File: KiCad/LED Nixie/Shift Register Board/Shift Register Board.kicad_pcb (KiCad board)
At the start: 2 copper layers, 25 x 25 mm, 10 parts, among them J1 Conn_01x04, J2 Conn_01x03, J3 Conn_01x03, J4 Conn_01x01, J5 Conn_01x01, J6 Shift, J7 +5V, J8 GND, U1 74HC595, U2 74HC595

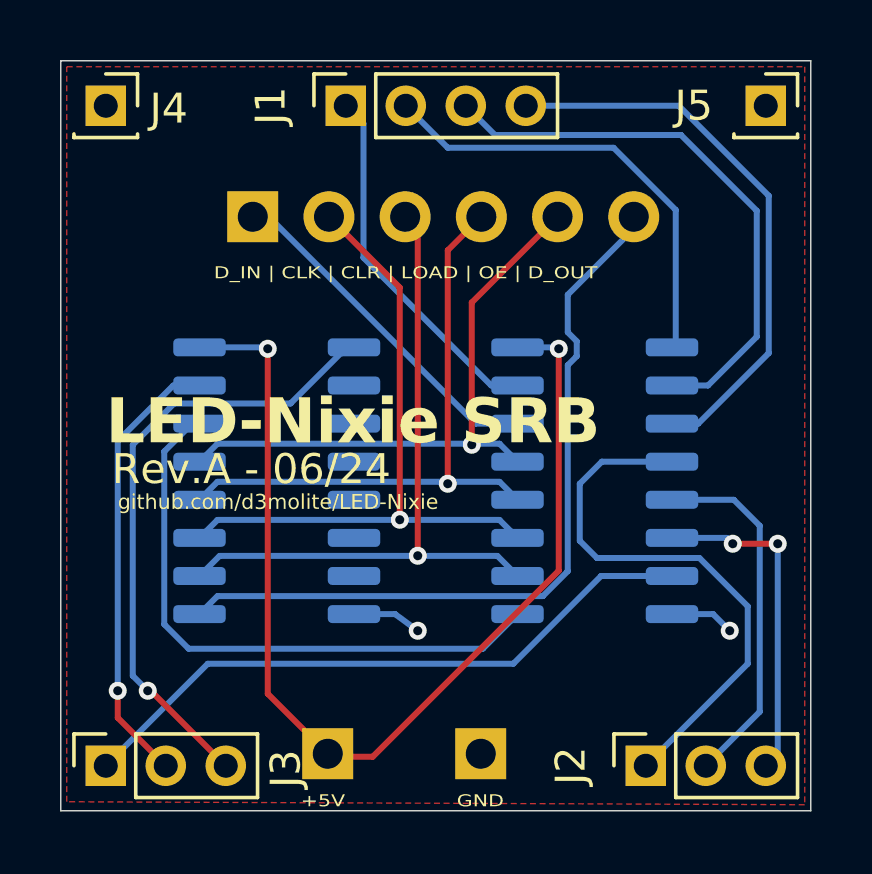
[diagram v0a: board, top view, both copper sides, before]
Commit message: added Decupling Caps
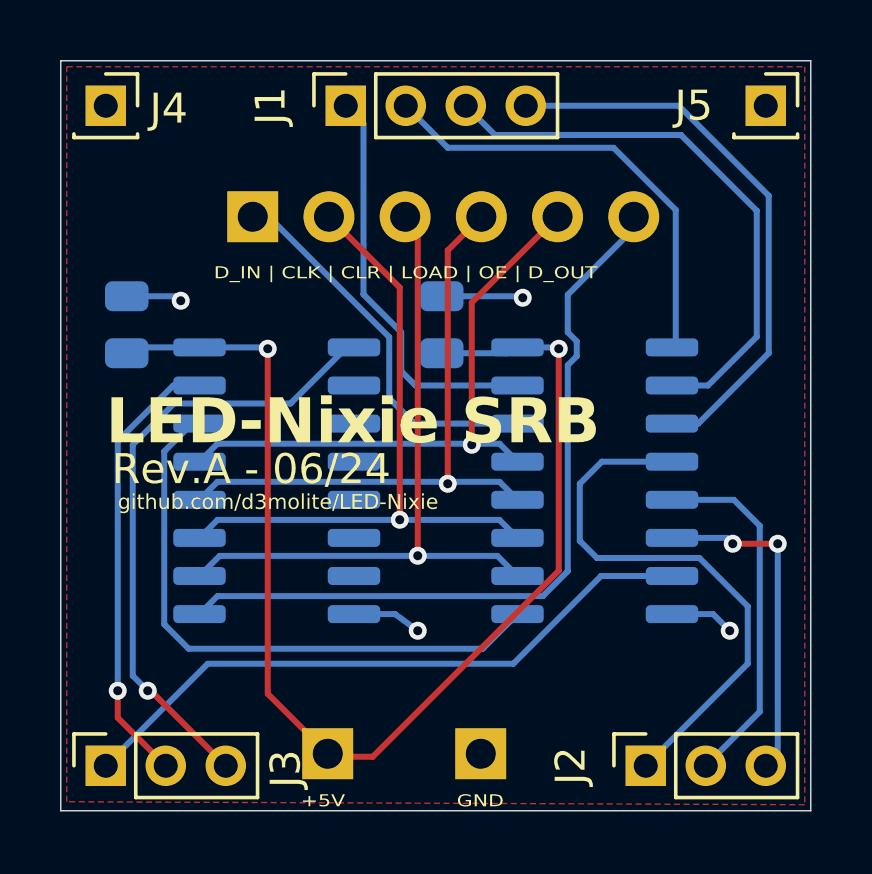
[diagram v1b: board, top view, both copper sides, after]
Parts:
- added C1: 10µF, Capacitor_SMD:C_0805_2012Metric, B.Cu at (52.7, 69.2)
- added C2: 10µF, Capacitor_SMD:C_0805_2012Metric, B.Cu at (63.2, 69.2)
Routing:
- net +5V: track 35.7 -> 40.8 mm
- net GND: track 4.66 -> 9.39 mm, vias 2 -> 4
- net Net-(J1-Pin_1): track 12.2 -> 13.7 mm
- net DATA: track 11.7 -> 12.9 mm
